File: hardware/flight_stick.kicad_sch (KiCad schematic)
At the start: 62 parts, among them J1 Load Cell 1, J10 USB_C_Receptacle_USB2.0, J11 Conn_01x05_Pin, J2 Conn_01x04_Male, J3 Load Cell 2, J5 Load Cell 3, J7 Conn_01x04_Male, J8 Conn_01x05_Pin, J9 Conn_ST_STDC14, Q4 2N7002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

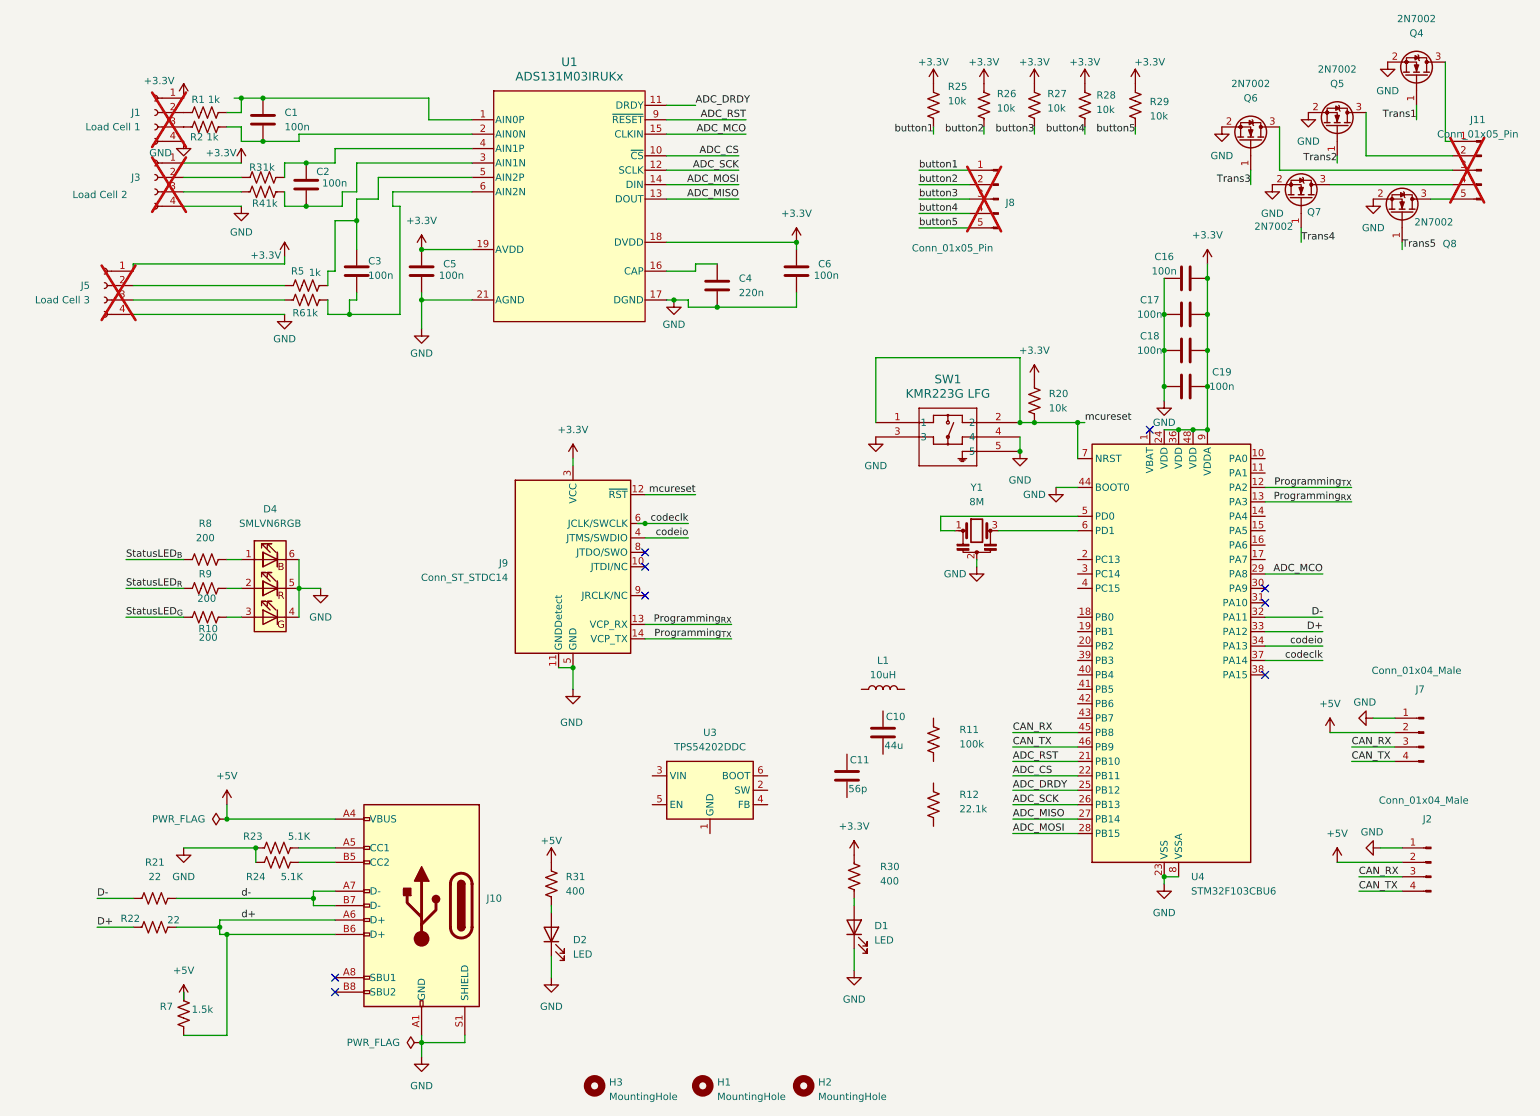
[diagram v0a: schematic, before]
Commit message: added new voltage reg
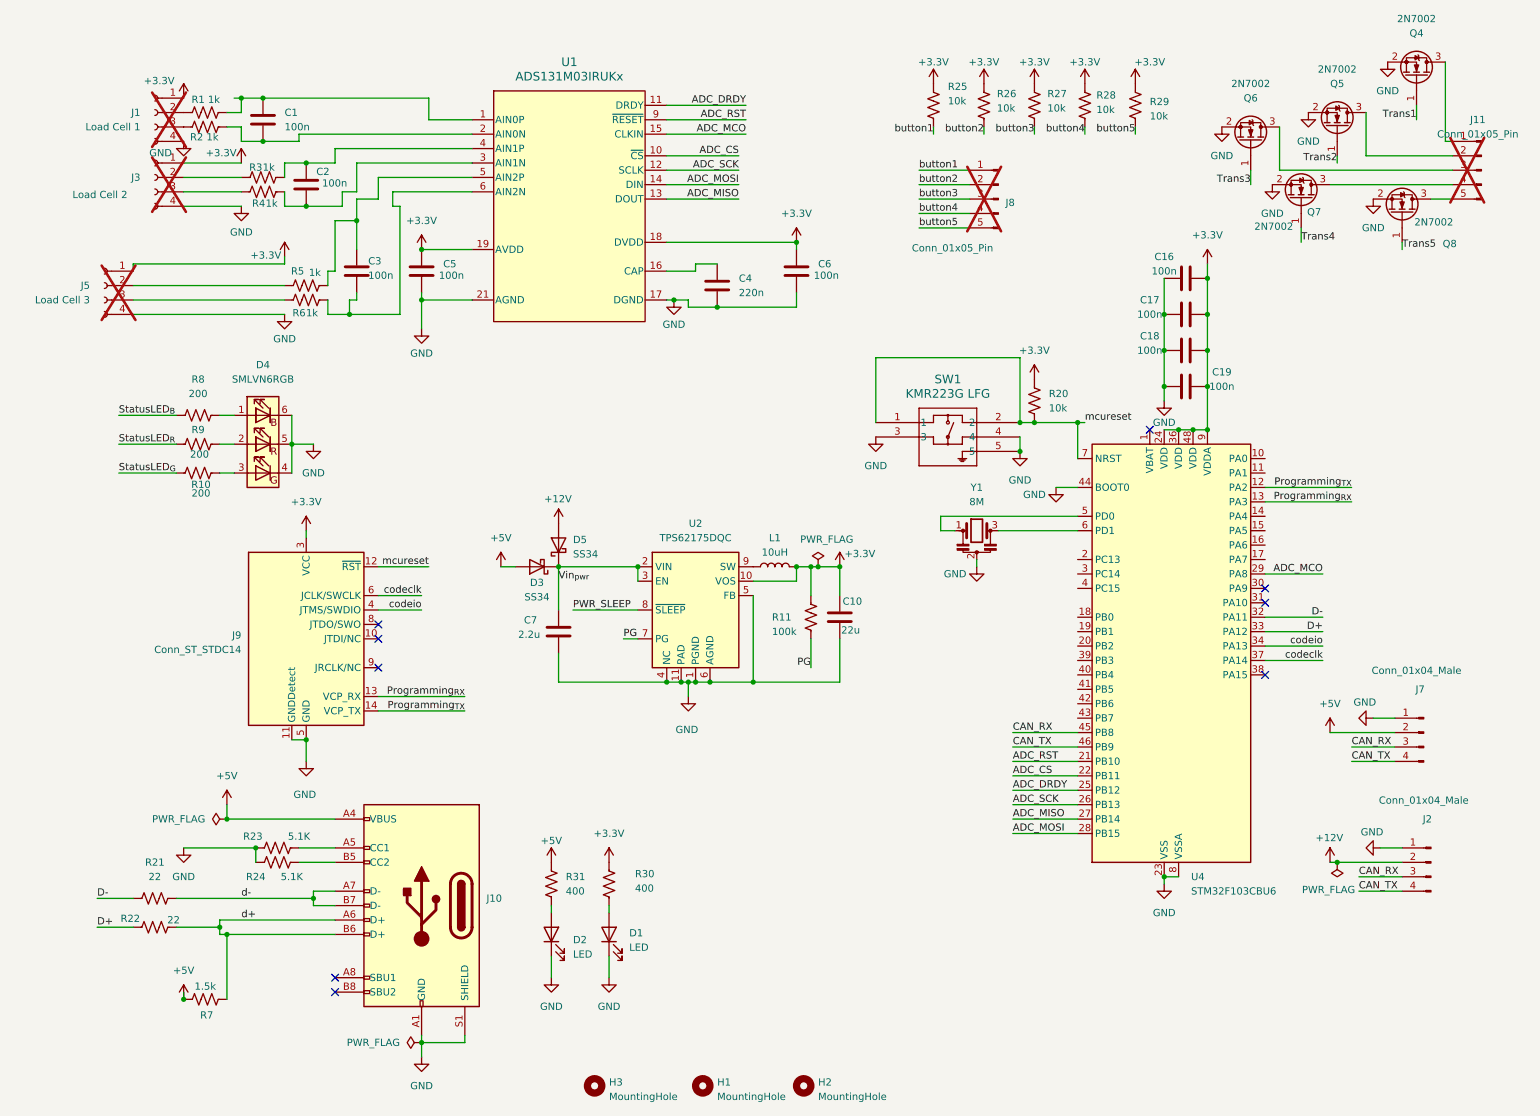
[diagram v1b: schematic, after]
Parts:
- removed C11: 56p, Capacitor_SMD:C_0603_1608Metric, symbol Device:C
- removed R12: 22.1k, Resistor_SMD:R_0603_1608Metric, symbol Device:R_US
- removed U3: TPS54202DDC, Package_TO_SOT_SMD:SOT-23-6, symbol Regulator_Switching:TPS54202DDC
- added C7: 2.2u, symbol Device:C
- added D3, D5: SS34, Diode_SMD:D_SMA, symbol Diode:SS34
- added U2: TPS62175DQC, Package_SON:WSON-10-1EP_2x3mm_P0.5mm_EP0.84x2.4mm_ThermalVias, symbol Regulator_Switching:TPS62175DQC
- C10: value 44u -> 22u
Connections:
- net +3.3V: now also C10.1, L1.2, R11.1, U2.10 (VOS)
- net +5V: now also D3.2 (A); no longer J2.2 (Pin_2)
- net AGND: now also C10.2, C7.2, U2.1 (PGND), U2.11 (PAD), U2.4 (NC), U2.5 (FB), U2.6 (AGND)
- net PG: now reaches R11.2
- net PG: now also U2.7 (PG)
- net at L1.1: now also U2.9 (SW)
- new net +12V: D5.2 (A), J2.2 (Pin_2)
- new net PWR_SLEEP: U2.8 (~{SLEEP})
- new net Vin_{pwr}: C7.1, D3.1 (K), D5.1 (K), U2.2 (VIN), U2.3 (EN)
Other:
- moved on the sheet: C10, D1, D4, J9, L1, R10, R11, R30, R7, R8, R9

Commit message: Added subpages and CAN tranciever
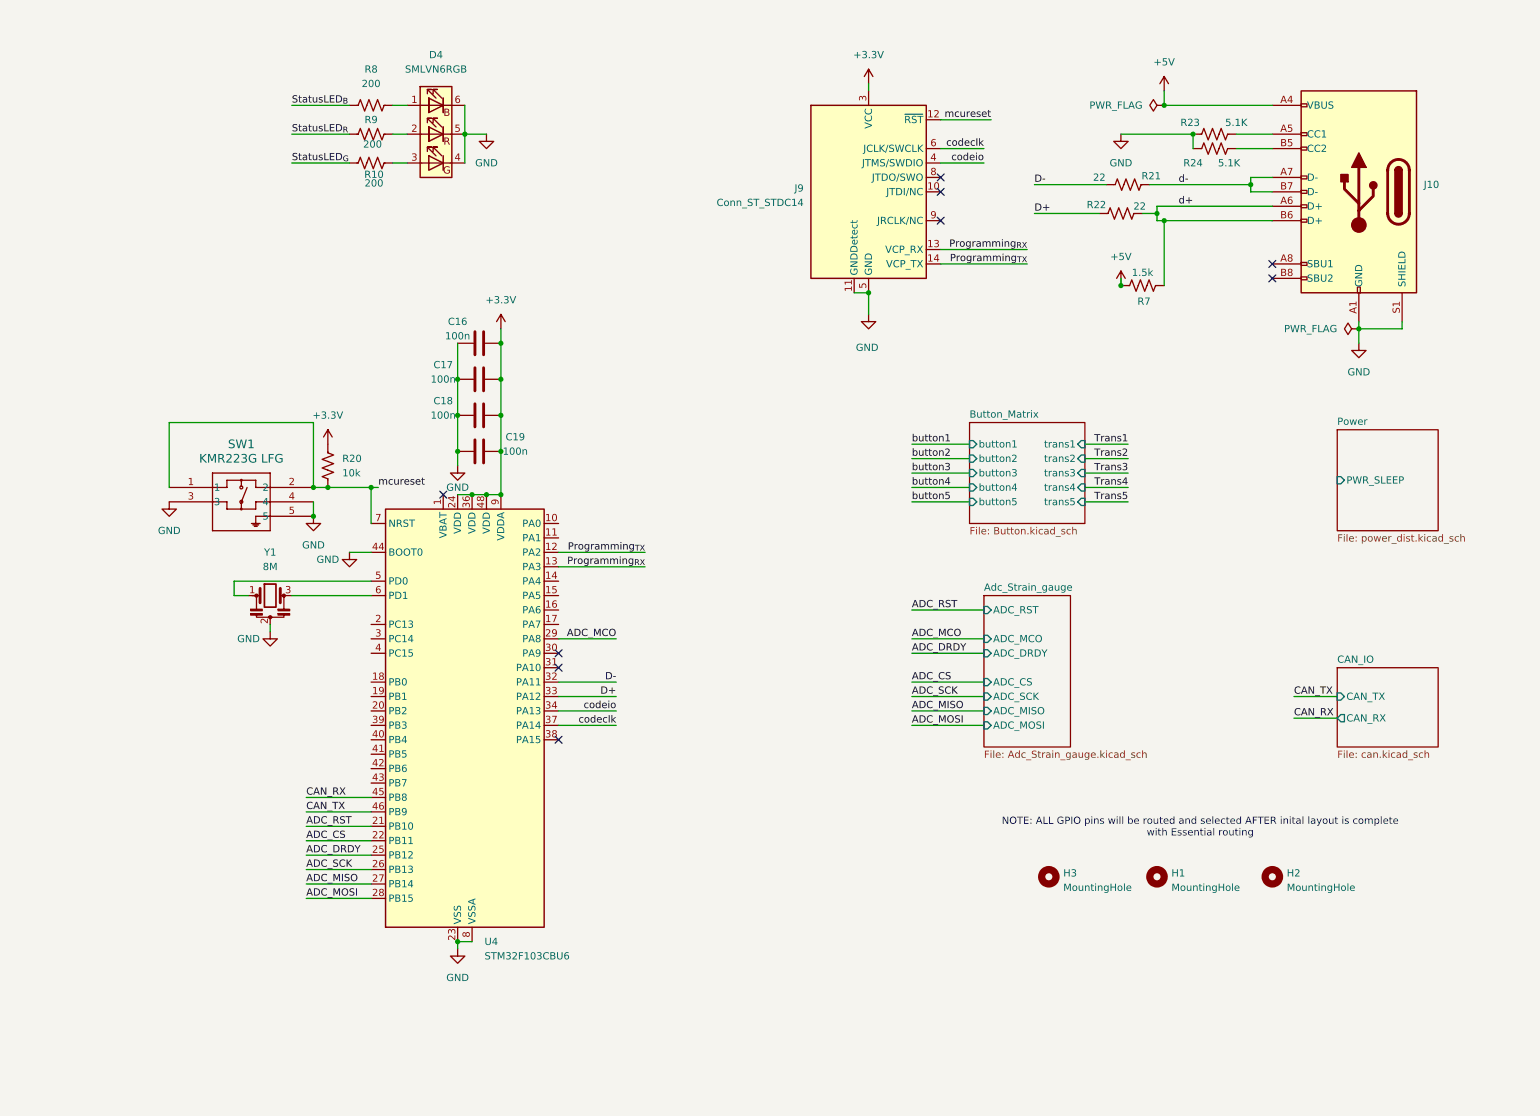
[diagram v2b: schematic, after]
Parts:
- removed C1, C2, C3, C5, C6: 100n, Capacitor_SMD:C_0603_1608Metric, symbol Device:C
- removed C10: 22u, Capacitor_SMD:C_0603_1608Metric, symbol Device:C
- removed C4: 220n, Capacitor_SMD:C_0603_1608Metric, symbol Device:C
- removed C7: 2.2u, symbol Device:C
- removed D1, D2: LED, LED_SMD:LED_0805_2012Metric, symbol Device:LED
- removed D3, D5: SS34, Diode_SMD:D_SMA, symbol Diode:SS34
- removed J1: Load Cell 1, Connector_PinHeader_1.27mm:PinHeader_1x04_P1.27mm_Vertical, symbol Connector:Conn_01x04_Socket
- removed J11, J8: Conn_01x05_Pin, Connector_PinHeader_2.54mm:PinHeader_1x05_P2.54mm_Vertical, symbol Connector:Conn_01x05_Pin
- removed J2, J7: Conn_01x04_Male, Connector_JST:JST_XH_B4B-XH-A_1x04_P2.50mm_Vertical, symbol Connector:Conn_01x04_Pin
- removed J3: Load Cell 2, Connector_PinHeader_1.27mm:PinHeader_1x04_P1.27mm_Vertical, symbol Connector:Conn_01x04_Socket
- removed J5: Load Cell 3, Connector_PinHeader_1.27mm:PinHeader_1x04_P1.27mm_Vertical, symbol Connector:Conn_01x04_Socket
- removed L1: 10uH, symbol Device:L
- removed Q4, Q5, Q6, Q7, Q8: 2N7002, Package_TO_SOT_SMD:SOT-23, symbol Transistor_FET:2N7002
- removed R1, R2, R3, R4, R5, R6: 1k, Resistor_SMD:R_0603_1608Metric, symbol Device:R_US
- removed R11: 100k, Resistor_SMD:R_0603_1608Metric, symbol Device:R_US
- removed R25, R26, R27, R28, R29: 10k, Resistor_SMD:R_0603_1608Metric, symbol Device:R_US
- removed R30, R31: 400, Resistor_SMD:R_0603_1608Metric, symbol Device:R_US
- removed U1: ADS131M03IRUKx, flight_stick_footprints:QFN_WQFN_RUK_TEX, symbol flight_stick:ADS131M03IRUKx
- removed U2: TPS62175DQC, Package_SON:WSON-10-1EP_2x3mm_P0.5mm_EP0.84x2.4mm_ThermalVias, symbol Regulator_Switching:TPS62175DQC
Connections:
- net AGND renamed GND
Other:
- added sheet Adc_Strain_gauge (Adc_Strain_gauge.kicad_sch)
- added sheet Button_Matrix (Button.kicad_sch)
- added sheet CAN_IO (can.kicad_sch)
- added sheet Power (power_dist.kicad_sch)
- note added: "NOTE: ALL GPIO pins will be routed and selected AFTER inital layout is complete with Essential routing"
- moved on the sheet: C16, C17, C18, C19, D4, H1, H2, H3, J10, J9, R10, R20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

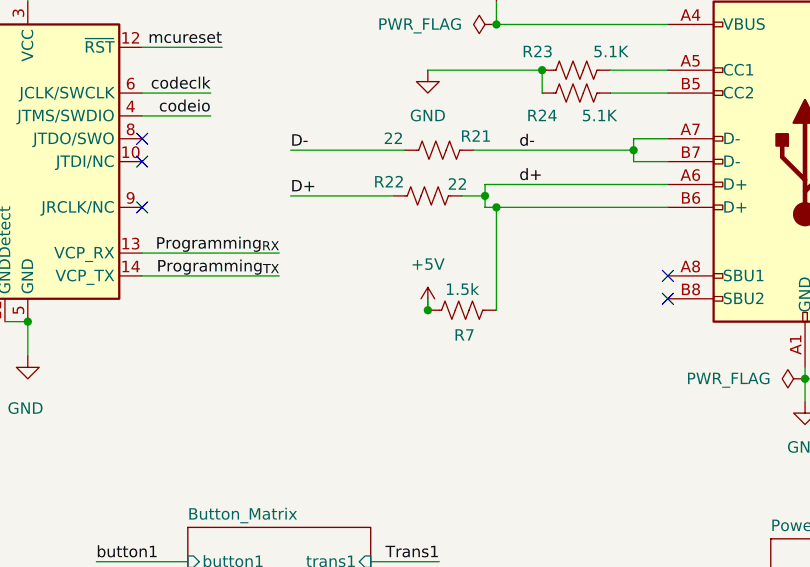
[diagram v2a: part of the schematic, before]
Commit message: Fixed ERC errors & CAN module
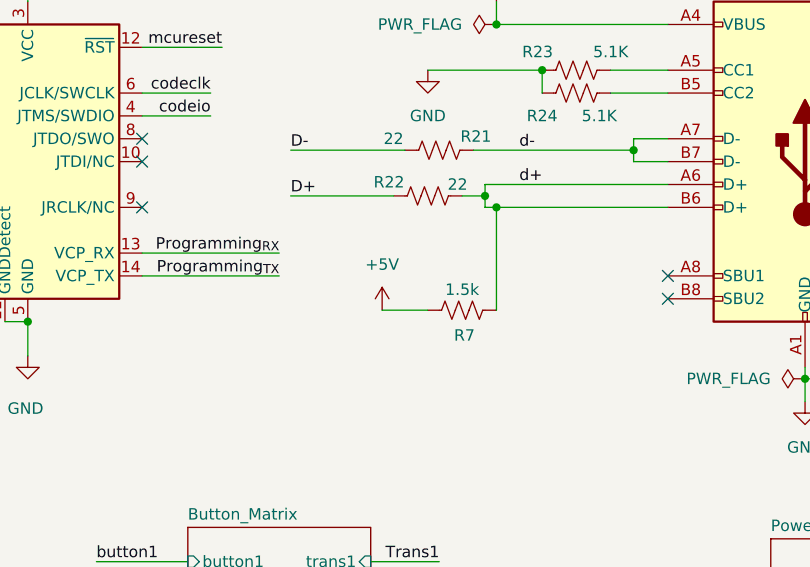
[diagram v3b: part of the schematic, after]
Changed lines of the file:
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@@
-	)
-	(junction
-		(at 198.12 59.69)
-		(diameter 0)
-		(color 0 0 0 0)
 	)
 	(junction
@@
 	(wire
 		(pts
+			(xy 193.04 59.69) (xy 198.12 59.69)
+		)
+		(stroke
+			(width 0)
+			(type default)
+		)
+	)
+	(wire
+		(pts
 			(xy 66.04 95.25) (xy 67.31 95.25)
 		)
@@
 		(pts
 			(xy 161.29 95.25) (xy 171.45 95.25)
-		)
-		(stroke
-			(width 0)
-			(type default)
-		)
-	)
-	(wire
-		(pts
-			(xy 198.12 58.42) (xy 198.12 59.69)
 		)
 		(stroke
@@
 	(symbol
 		(lib_id "power:+5V")
-		(at 198.12 59.69 0)
+		(at 193.04 59.69 0)
 		(unit 1)
 		(exclude_from_sim no)
@@
 		(fields_autoplaced yes)
 		(property "Reference" "#PWR06"
-			(at 198.12 63.5 0)
+			(at 193.04 63.5 0)
 			(effects
 				(font
@@
 		)
 		(property "Value" "+5V"
-			(at 198.12 54.61 0)
+			(at 193.04 54.61 0)
 			(effects
 				(font
@@
 		)
 		(property "Footprint" ""
-			(at 198.12 59.69 0)
+			(at 193.04 59.69 0)
 			(effects
 				(font
@@
 		)
 		(property "Datasheet" ""
-			(at 198.12 59.69 0)
+			(at 193.04 59.69 0)
 			(effects
 				(font
@@
 		)
 		(property "Description" "Power symbol creates a global label with name \"+5V\""
-			(at 198.12 59.69 0)
+			(at 193.04 59.69 0)
 			(effects
 				(font
